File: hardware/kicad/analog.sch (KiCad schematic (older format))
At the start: 13 parts, among them U2 MCP6492

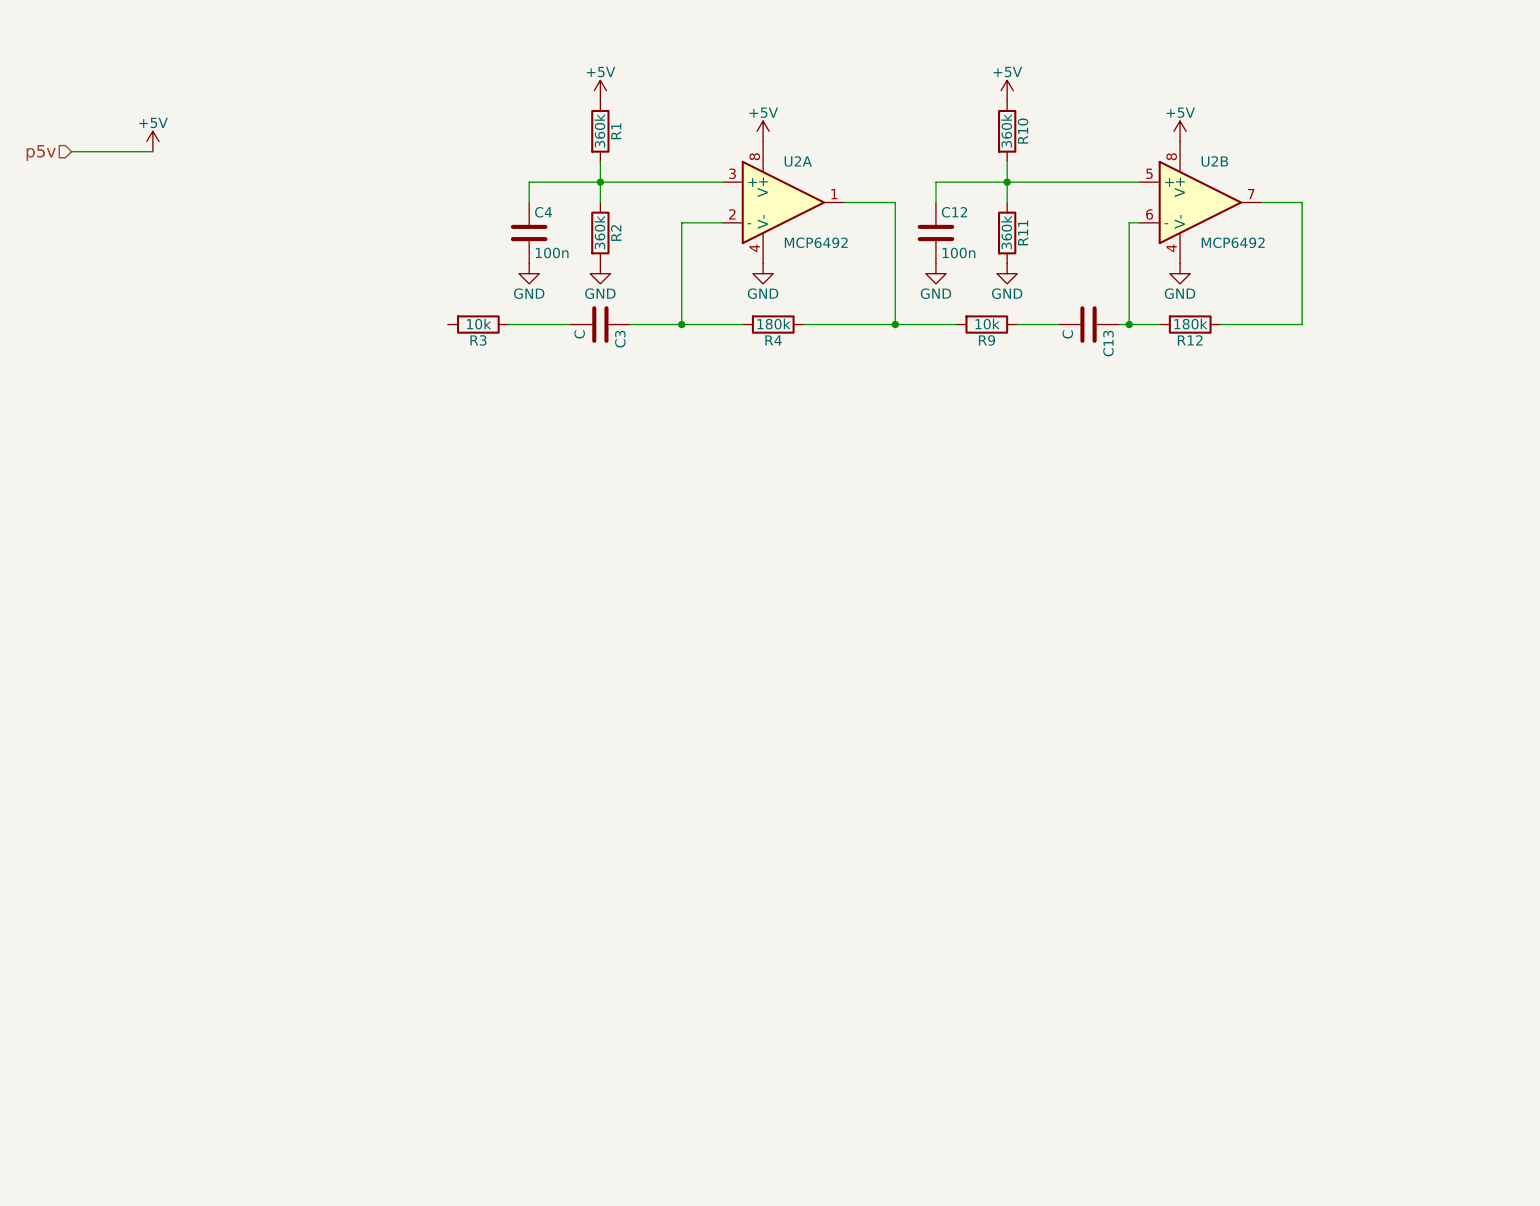
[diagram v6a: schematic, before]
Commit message: Updated schematic and PCB.
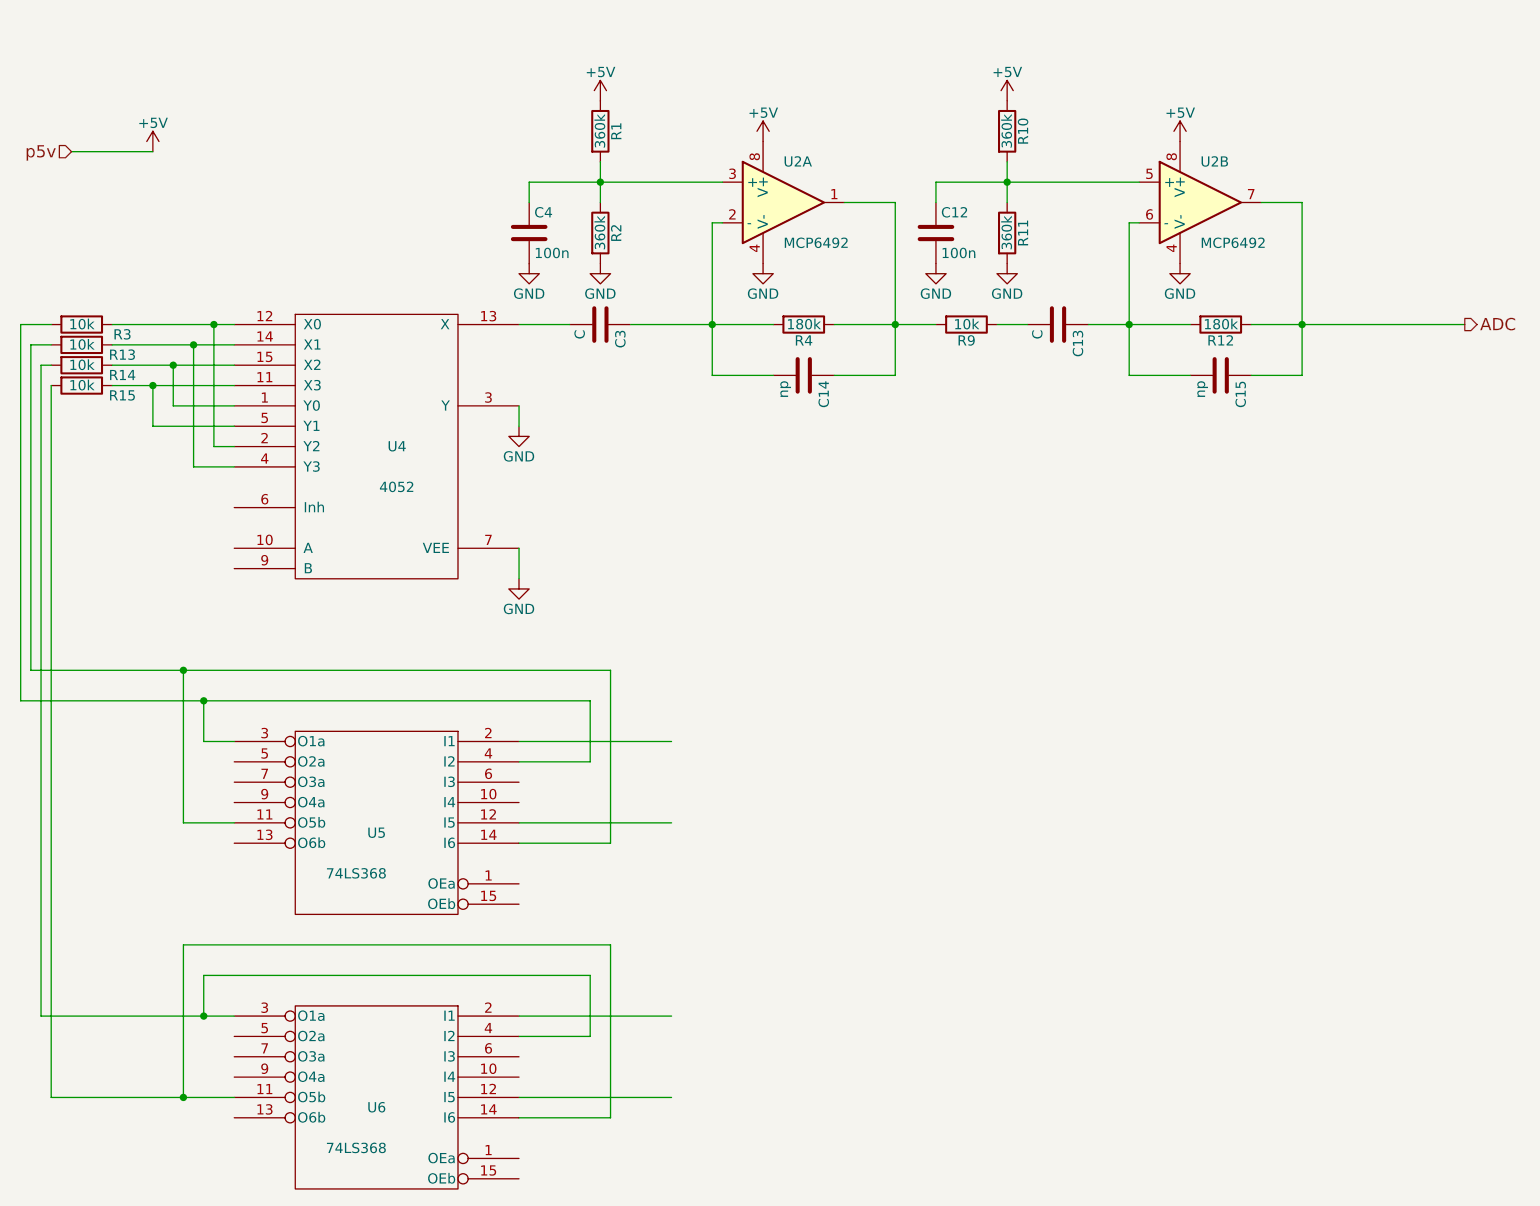
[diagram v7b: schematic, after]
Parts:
- added C14, C15: np, Capacitors_SMD:C_0805_HandSoldering, symbol C
- added R13, R14, R15: 10k, Resistors_SMD:R_0805_HandSoldering, symbol R
- added U4: 4052, Housings_DIP:DIP-16_W7.62mm_LongPads, symbol 4052
- added U5, U6: 74LS368, Housings_DIP:DIP-16_W7.62mm_LongPads, symbol 74LS368
- U2: footprint (none) -> Housings_SOIC:SOIC-8_3.9x4.9mm_Pitch1.27mm
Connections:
- net labels added: ADC
- wire segments 21 -> 70
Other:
- moved on the sheet: C13, R12, R3, R4, R9
